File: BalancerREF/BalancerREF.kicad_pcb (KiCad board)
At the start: 4 copper layers, 50 x 50 mm, 89 parts, among them J1 USB4105-GF-A, J2 LiPo 500mAh PROTECTED, J3 MAG+ / MAG- PTH, J4 GPS MODULE 3V3 UART, J5 OPTICAL HEAD 7-WAY, Q4 AO3401A, SW1 POWER, SW2 ACQUIRE, SW3 BOOT / SERVICE, U1 ESP32-S3-MINI-1-N8, U10 SN74LVC1G123DCTR, U2 IIS3DWBTR, U3 LM1815MX/NOPB, U5 BQ24075RGT, U6 TPS63031DSKR, U7 SRV05-4MR6T1G, U9 SN74LVC1G132DBVR

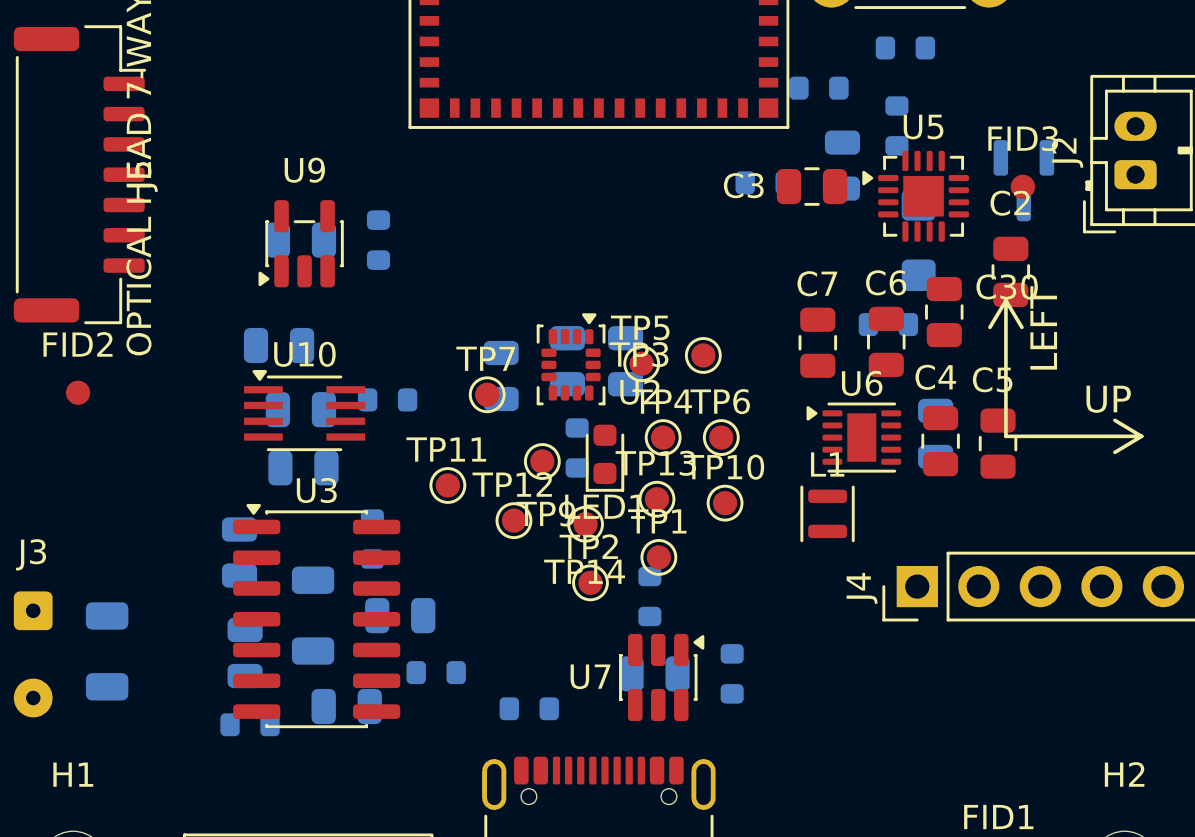
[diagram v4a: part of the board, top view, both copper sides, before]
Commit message: fix: U9 sourcing metadata, capacitor pin targets, charger docs
Three review comments on PR #2, all three valid.

U9 sourcing still said SN74LVC1G08 (P1). The Value field was swapped but the
footprint's Datasheet and MPN properties, PhotoTach-BOM.csv and the JLCPCB
checklist all still named the AND gate. An MPN-driven order would have populated
a part the circuit no longer works with - U10 is wired for the NAND polarity and
the whole point of the swap is the Schmitt inputs. All four updated, plus the
Rev C pin-audit line marked superseded so it is not read as current.

While chasing that: the schematic's lib_symbols cache still held definitions for
seven parts no longer on the sheet, including MCP73831-2-OT and D_Schottky from
the charger swap and 74LVC1G08 from this one. KiCad ignores them, but each
carries a Value and Datasheet for a part that is not fitted, which is the same
stale-sourcing hazard. scripts/prune_symbol_cache.py removes entries with zero
referencing instances and proves the netlist is unchanged.

Capacitors aimed at the net, not the pin (P2). U6 pins 5-8 are all on SYS_SW, so
targeting the input net put the caps beside EN and PS/SYNC - logic inputs that
happen to be strapped high - instead of VIN and VINA. The 10u bulk had also taken
the close spot while the 100n sat 4.4 mm out. Now C5 is 2.07 mm from VINA and C4
2.68 mm from VIN, and the script carries the pin-function map so the report names
the pin it aimed at. Same error had C6 aimed at FB rather than VOUT.

Two things that check found on its own:
  * C1, the 100n bypass on the BQ24075 IN pin, was 24 mm away on the BACK of the
    board - the same as not fitting it. Now 5.3 mm out on the front.
  * TP6 and TP10 sat immediately left of U6, the side VIN and PGND are on, and
    were why the bulk input cap could not reach its pins. A probe pad has no
    business crowding a 2.4 MHz input loop; both moved beside the signal they
    actually probe and are nearer it than before.

Charger documentation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
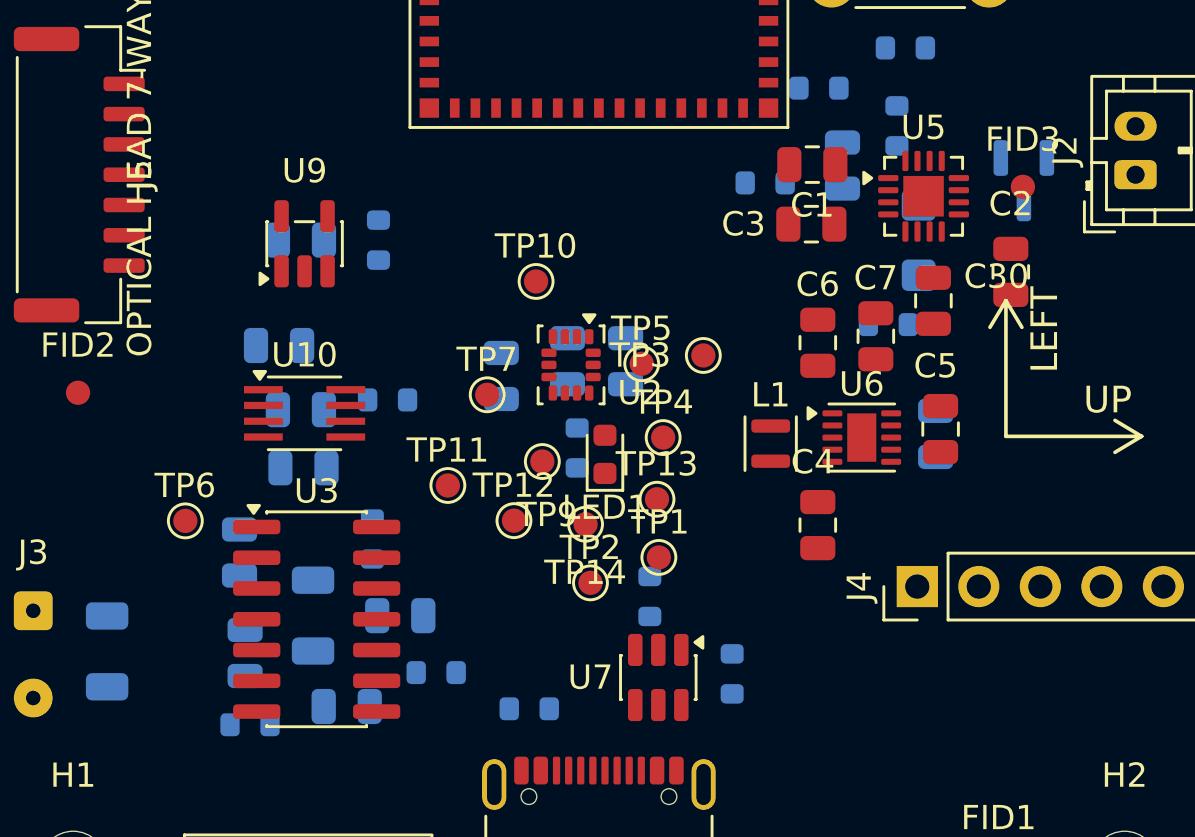
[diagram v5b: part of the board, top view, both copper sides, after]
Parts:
- C1: moved to F.Cu
- moved TP6 22.4 mm to (107.9, 132.3)
- moved C1 22.0 mm to (133.8, 117.6), turned to 180 degrees
- moved TP10 12.0 mm to (122.4, 122.4)
- moved C4 6.14 mm to (134.0, 132.5)
- moved L1 3.73 mm to (132.1, 129.1)
- moved C6 2.83 mm to (134.0, 124.9)
- moved C5 2.44 mm to (139.1, 128.5)
- moved C7 2.41 mm to (136.4, 124.7)
- moved C3 1.55 mm to (133.8, 120.0)
- moved C30 0.65 mm to (138.8, 123.2)

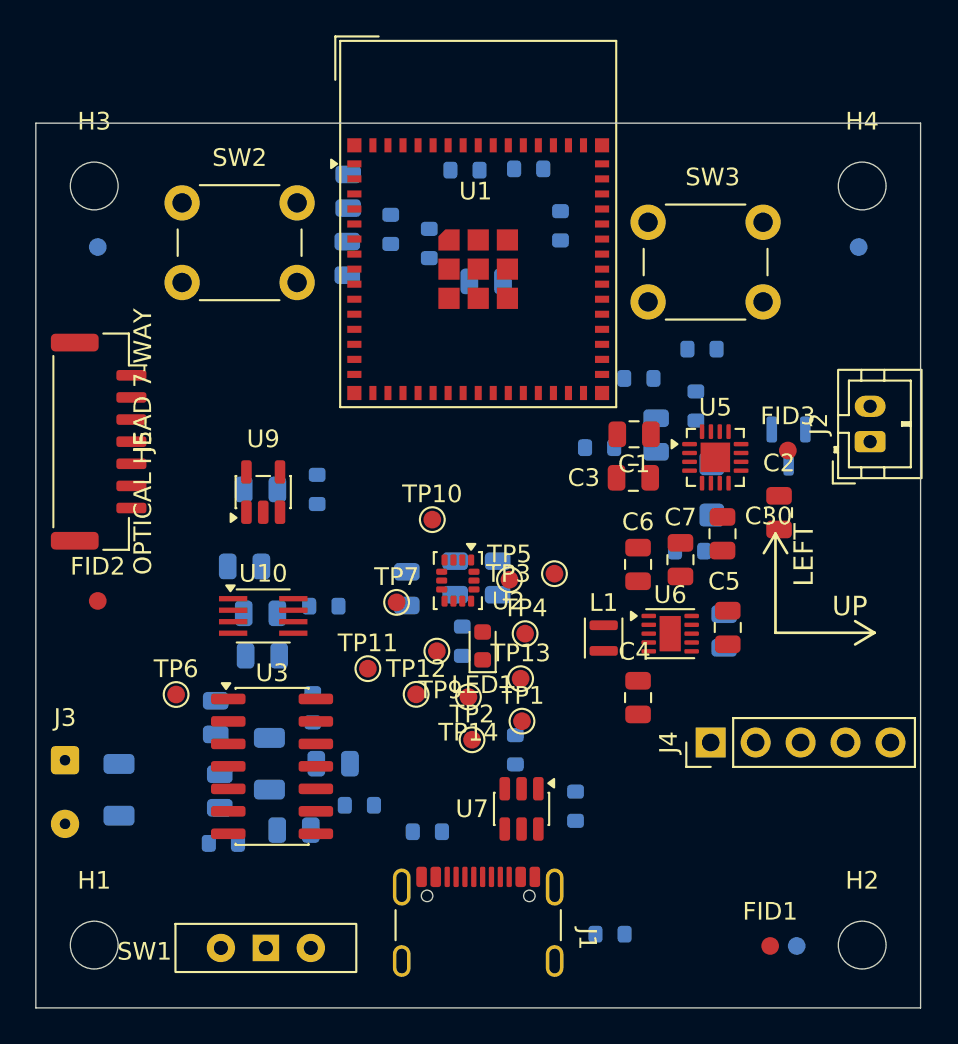
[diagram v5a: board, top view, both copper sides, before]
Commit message: feat: BalancerREF regrouped placement, hand routing, neck-down rules
Board: power chain regrouped into the top-right corner (U5 beside J2, U6
below it, SW1 on the right edge), USB channel cleared between J1 and U1,
passives re-clustered under their ICs. Seven test points dropped
(TP4/5/6/11/12/13/14). First pass of hand routing.

Rules: BalancerREF.kicad_dru necks Power-class tracks down to 0.2 mm and
vias to 0.5/0.3 inside the 0.5 mm pitch packages (U5, U6, U2, U10) and
0.3 mm in the SOT-23s (U7, U9).

Scripts: regroup_blocks.py (the placement pass, dry run by default) and
recover_from_dsn.py, which replays a Freerouting DSN export back onto the
saved board - used to recover the 22:00 session after the editor crashed
on session import.

Co-Authored-By: Claude Fable 5.1 <noreply@anthropic.com>
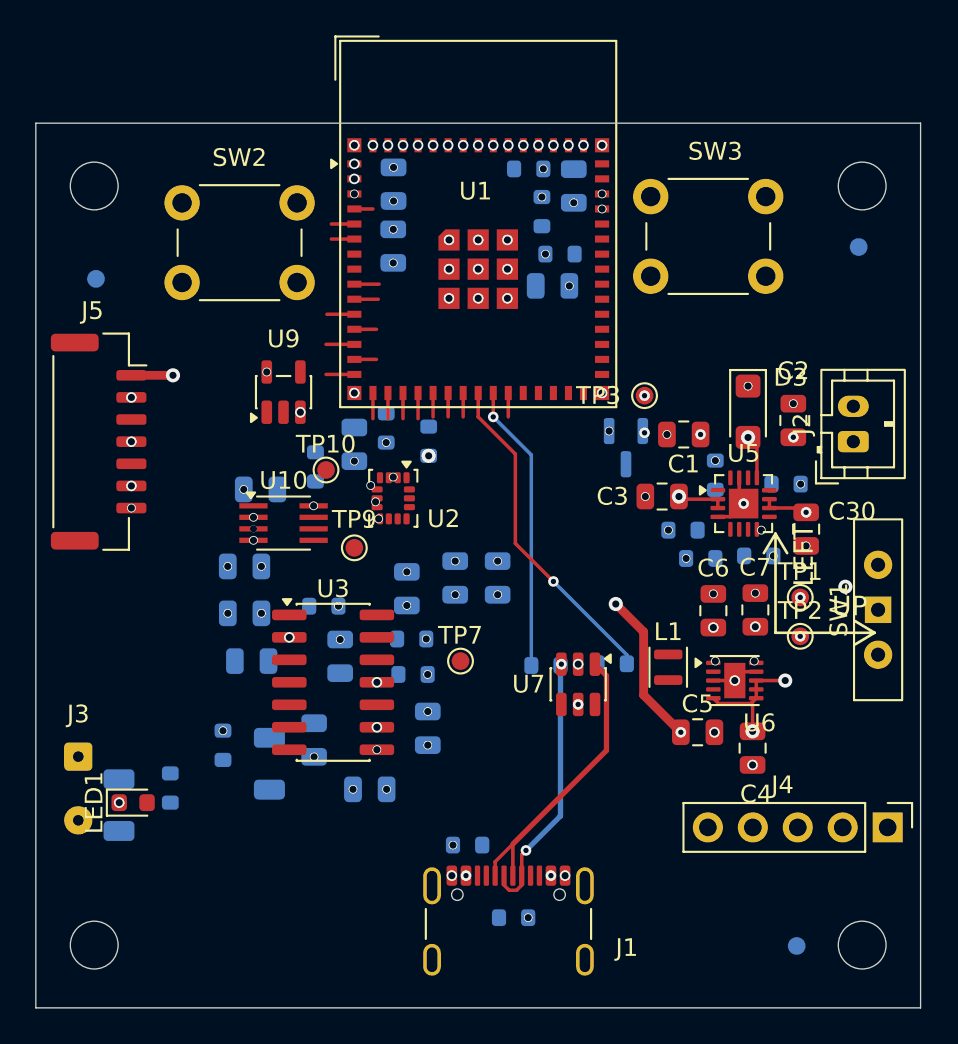
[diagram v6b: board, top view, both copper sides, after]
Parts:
- removed FID1, FID2, FID3: FIDUCIAL, Fiducial_1mm_Mask2mm
- removed TP11: TP_USB_D+, TestPoint:TestPoint_Pad_D1.0mm
- removed TP12: TP_USB_D-, TestPoint:TestPoint_Pad_D1.0mm
- removed TP13: TP_EN, TestPoint:TestPoint_Pad_D1.0mm
- removed TP14: TP_BOOT, TestPoint:TestPoint_Pad_D1.0mm
- removed TP4: TP_USB_VBUS, TestPoint:TestPoint_Pad_D1.0mm
- removed TP5: TP_MAG+, TestPoint:TestPoint_Pad_D1.0mm
- removed TP6: TP_MAG-, TestPoint:TestPoint_Pad_D1.0mm
- D3: moved to F.Cu
- moved SW1 39.5 mm to (147.6, 127.5), turned to 90 degrees
- moved C12 23.4 mm to (118.0, 118.2)
- moved LED1 21.6 mm to (105.5, 138.4), turned to 0 degrees
- moved TP2 19.4 mm to (143.2, 129.0)
- moved R10 18.5 mm to (107.6, 137.6)
- moved TP1 17.2 mm to (143.2, 126.8)
- moved R16 15.7 mm to (121.2, 129.2)
- moved R11 15.5 mm to (122.2, 118.0), turned to 90 degrees
- moved C10 14.8 mm to (130.4, 103.5)
- moved R37 11.8 mm to (137.6, 124.6), turned to 0 degrees
- moved TP3 11.3 mm to (134.4, 115.4)
- moved J4 11.1 mm to (148.1, 139.8), turned to -90 degrees
- moved R38 10.9 mm to (140.9, 124.5)
- moved R12 10.7 mm to (119.8, 117.2)
- moved R4 9.67 mm to (129.6, 107.4), turned to 0 degrees
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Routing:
- net /SYS_SW: track 0.00 -> 59.0 mm, vias 0 -> 8
- net /USB_VBUS: track 0.00 -> 42.0 mm, vias 0 -> 7
- net Net-(U1-USB_D-): track 0.00 -> 18.8 mm, vias 0 -> 1
- net /USB_CONN_D-: track 0.00 -> 16.6 mm
- net Net-(U1-USB_D+): track 0.00 -> 16.3 mm, vias 0 -> 1
- net /USB_CONN_D+: track 0.00 -> 15.1 mm, vias 0 -> 2
- net /SYS: track 0.00 -> 10.2 mm, vias 0 -> 3
- net /BAT: track 0.00 -> 9.27 mm, vias 0 -> 4
- net GND: track 0.00 -> 5.96 mm, vias 0 -> 82
- net /STATUS_LED: track 0.00 -> 1.60 mm
- net /OPT_LED_EN: track 0.00 -> 1.60 mm
- net /MAG_TACH: track 0.00 -> 1.55 mm
- net /SUPPLY_SENSE: track 0.00 -> 1.45 mm
- net /GPS_PPS: track 0.00 -> 1.45 mm
- net /ACCEL_SCK: track 0.00 -> 1.45 mm
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- added copper zone on In2.Cu, net /+3V3
- added copper zone on In1.Cu, net GND

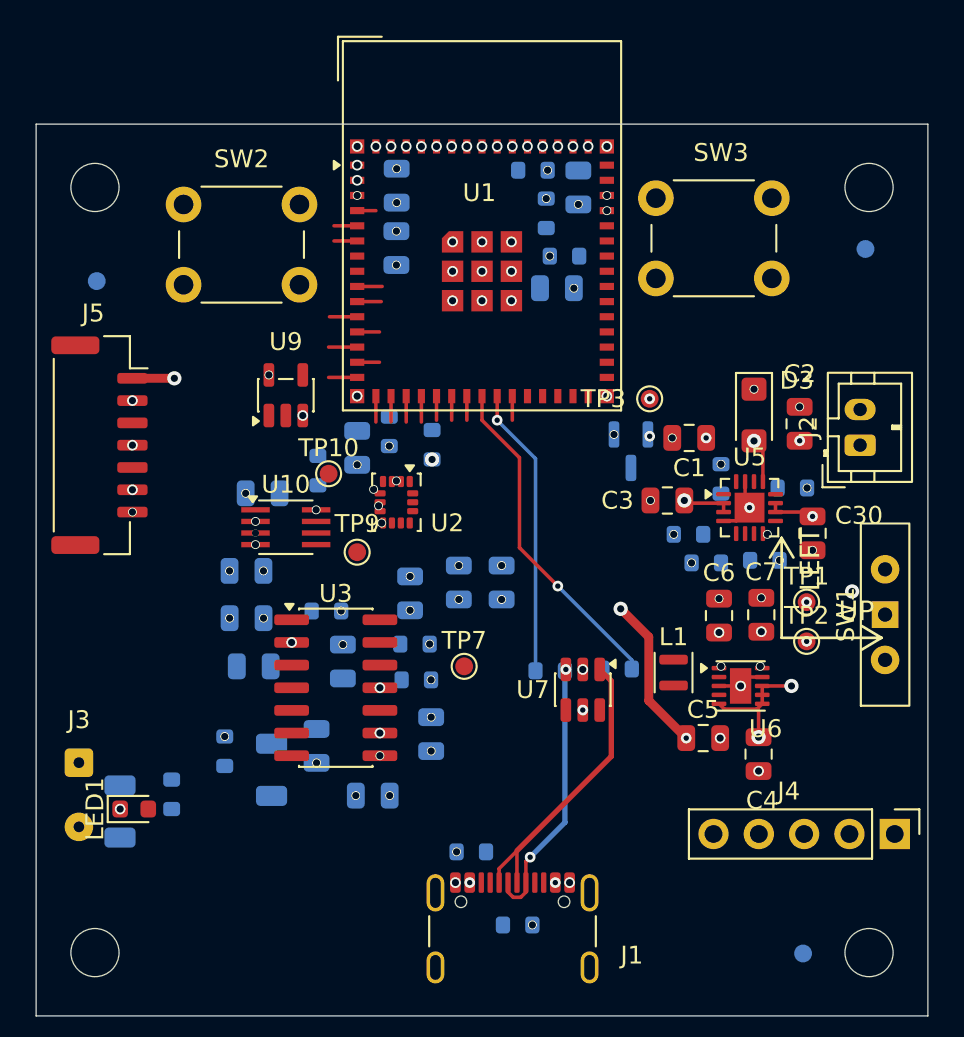
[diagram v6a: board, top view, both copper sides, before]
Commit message: feat: BalancerREF routing progress after the autorouter rollback
Continued hand routing on the regrouped placement, saved after
restoring the pre-autoroute state.

Co-Authored-By: Claude Fable 5.1 <noreply@anthropic.com>
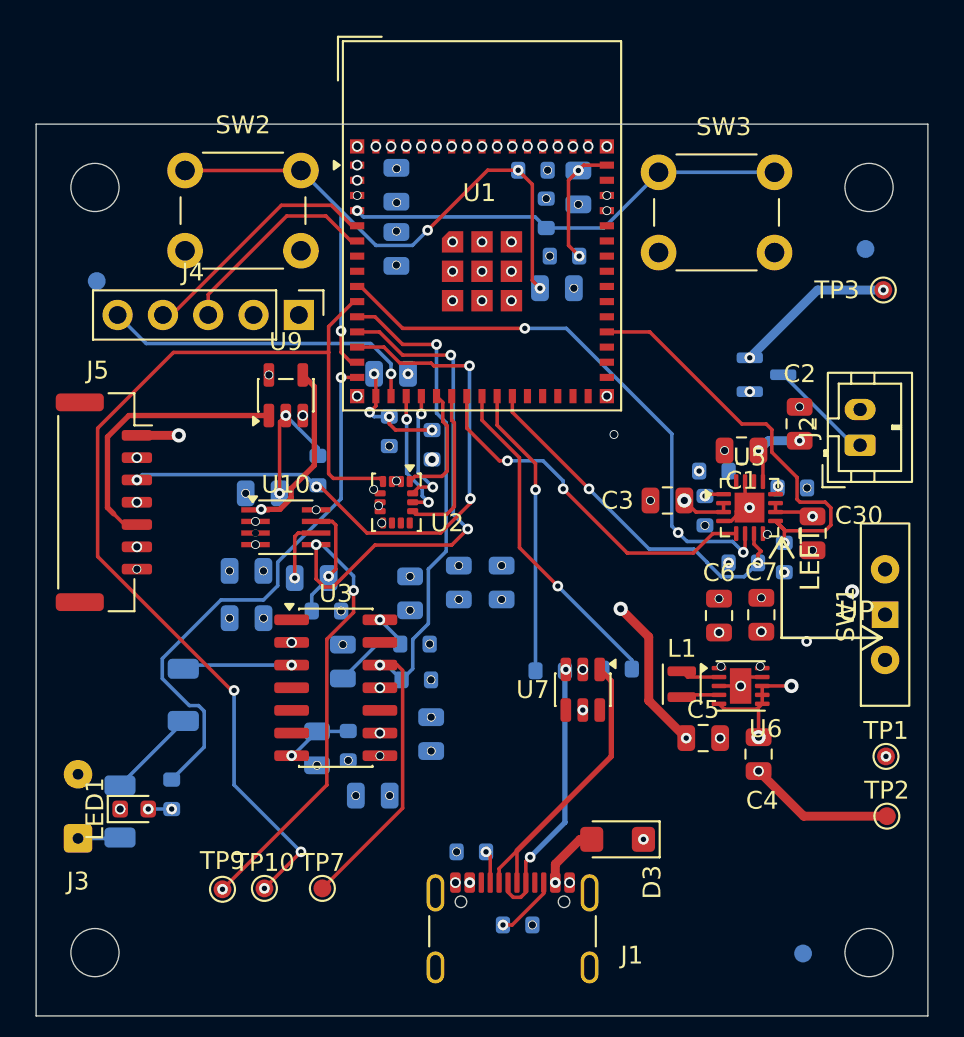
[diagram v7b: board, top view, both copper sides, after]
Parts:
- moved J4 44.3 mm to (114.7, 110.7)
- moved D3 25.0 mm to (132.6, 140.1), turned to 180 degrees
- moved TP10 23.5 mm to (112.8, 142.8)
- moved TP9 20.4 mm to (110.5, 142.9)
- moved TP7 14.8 mm to (116.0, 142.8)
- moved TP3 14.5 mm to (147.5, 109.3)
- moved TP2 10.8 mm to (147.7, 138.8)
- moved TP1 9.73 mm to (147.7, 135.4)
- moved Q4 8.73 mm to (140.9, 114.0), turned to 0 degrees
- moved R17 6.93 mm to (117.5, 134.8), turned to -90 degrees
- moved R14 6.49 mm to (108.2, 132.0)
- moved C28 5.92 mm to (115.5, 125.5), turned to 180 degrees
- moved C12 4.56 mm to (119.9, 114.0), turned to 0 degrees
- moved J3 4.25 mm to (102.3, 140.1), turned to 90 degrees
- moved C9 3.55 mm to (120.2, 107.0)
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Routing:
- net /ACCEL_DRDY: track 1.35 -> 59.8 mm, vias 0 -> 3
- net /OPT_TACH: track 1.25 -> 51.3 mm, vias 0 -> 5
- net /MAG_TACH: track 1.55 -> 42.2 mm, vias 0 -> 2
- net /ACQUIRE_BUTTON: track 1.25 -> 38.4 mm, vias 0 -> 4
- net /OPT_LED_EN: track 1.60 -> 35.3 mm, vias 0 -> 4
- net /CHG_EN1: track 1.40 -> 31.9 mm, vias 0 -> 3
- net /STATUS_LED: track 1.60 -> 31.0 mm, vias 0 -> 1
- net /BOOT: track 1.05 -> 25.1 mm, vias 0 -> 2
- net /CHG_STAT: track 0.00 -> 24.0 mm, vias 0 -> 1
- net /PGOOD_N: track 1.35 -> 20.7 mm, vias 0 -> 2
- net /CHG_EN2: track 1.35 -> 20.5 mm, vias 0 -> 2
- net /GPS_PPS: track 1.45 -> 18.3 mm, vias 0 -> 1
- net /BAT: track 9.27 -> 25.1 mm
- net /OPT_COMP: track 0.00 -> 15.6 mm
- net /GPS_UART_TX: track 1.30 -> 13.9 mm
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
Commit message: chore: update balancer board files and review tooling
Co-Authored-By: Claude Opus 5 (1M context) <noreply@anthropic.com>
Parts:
- C5: moved to B.Cu
- moved C19 2.02 mm to (114.3, 136.4)
- moved R6 1.15 mm to (132.5, 131.7), turned to 90 degrees
- moved R3 1.13 mm to (137.2, 118.7), turned to -90 degrees
- moved C5 0.60 mm to (138.0, 134.4), turned to -90 degrees
- moved C4 0.57 mm to (140.5, 134.8)
- moved L1 0.50 mm to (135.7, 131.4)
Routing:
- net /+3V3: track 0.00 -> 6.47 mm, vias 31 -> 29
- net /ISET: track 0.00 -> 3.31 mm, vias 0 -> 1
- net /SYS_SW: track 57.4 -> 54.6 mm, vias 8 -> 5
- net Net-(U10-~{A}): track 9.65 -> 10.4 mm, vias 1 -> 0
- net Net-(U6-L1): track 2.14 -> 2.66 mm
- net /OPT_TACH: track 51.3 -> 51.7 mm, vias 5 -> 4
- net /BOOT: track 25.1 -> 25.5 mm, vias 2 -> 1
- net GND: track 14.3 -> 14.7 mm, vias 83 -> 81
- net /USB_CONN_D-: track 16.6 -> 16.8 mm, vias 0 -> 1
- net Net-(LED1-A): vias 2 -> 1
- net /SYS: vias 3 -> 1
- net /CHG_EN1: vias 3 -> 2
- net /BAT: vias 4 -> 3
- net /ACCEL_DRDY: vias 3 -> 2
